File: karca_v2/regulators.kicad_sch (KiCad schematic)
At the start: 27 parts, among them J1 CON_FAN1, J2 Conn_Batt, J3 USB_B_Micro, Q1 AO3401A, SW1 SW_SPST, SW2 SW_SPST, SW3 SW_SPST, U1 TVS1400DRV

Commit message: fixed pmos
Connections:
- net +5V: now also Q1.2 (S); no longer Q1.3 (D)
- net at D4.2 (A), J3.1 (VBUS), TP5.1: now also Q1.3 (D); no longer Q1.2 (S)
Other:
- moved on the sheet: Q1
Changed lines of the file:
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@@
     )
   )
-  (symbol (lib_id "Simulation_SPICE:PMOS") (at 381 157.48 270) (unit 1)
+  (symbol (lib_id "Simulation_SPICE:PMOS") (at 381 157.48 90) (mirror x) (unit 1)
     (in_bom yes) (on_board yes) (dnp no)
     (property "Reference" "Q1" (at 381 163.957 90)
@@
       (effects (font (size 1.27 1.27)))
     )
-    (property "Footprint" "AO3401A:SOT23-3" (at 383.54 162.56 0)
+    (property "Footprint" "AO3401A:SOT23-3" (at 378.46 162.56 0)
       (effects (font (size 1.27 1.27)) hide)
     )
-    (property "Datasheet" "https://ngspice.sourceforge.io/docs/ngspice-manual.pdf" (at 368.3 157.48 0)
+    (property "Datasheet" "https://ngspice.sourceforge.io/docs/ngspice-manual.pdf" (at 393.7 157.48 0)
       (effects (font (size 1.27 1.27)) hide)
     )
-    (property "Sim.Device" "PMOS" (at 363.855 157.48 0)
+    (property "Sim.Device" "PMOS" (at 398.145 157.48 0)
       (effects (font (size 1.27 1.27)) hide)
     )
-    (property "Sim.Type" "VDMOS" (at 361.95 157.48 0)
+    (property "Sim.Type" "VDMOS" (at 400.05 157.48 0)
       (effects (font (size 1.27 1.27)) hide)
     )
-    (property "Sim.Pins" "1=D 2=G 3=S" (at 365.76 157.48 0)
+    (property "Sim.Pins" "1=D 2=G 3=S" (at 396.24 157.48 0)
       (effects (font (size 1.27 1.27)) hide)
     )

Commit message: Passed all DRC, Added safety jumper to isolate regulators from rest of the board
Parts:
- added JP5: Jumper_3_Bridged12, Connector_PinHeader_2.00mm:PinHeader_1x03_P2.00mm_Vertical, symbol Jumper:Jumper_3_Bridged12
- added R121: 250, Resistor_SMD:R_1206_3216Metric, symbol Device:R_US
- J3: footprint USB-B:GCT_USB3090-XX-X_REVE -> USB-B:USB_Micro-B_Molex-105017-0001
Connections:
- net +5V: now also JP5.3 (B); no longer D5.1 (K), Q1.2 (S)
- net GND: now also R121.2
- new net: JP5.2 (C), R121.1
- new net Jumper: D5.1 (K), JP5.1 (A), Q1.2 (S)
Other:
- note added: "Jumper is used to verify the power supply voltage before connecting it to the rest of the circuit"
- moved on the sheet: C1, C2, D1, D2, D3, D4, D5, F1, J1, J2, J3, MD1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

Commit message: cleaned up documentation. Added production files and BOM. Marked Thermocouple components and THT components as DNP (excluded them from BOM too) to match version sent to JLCPCB for fabrication
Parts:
- removed MD1: OKL-T_6-W12N-C, OKL-T6-W12N:MURATA_OKL-T-6-W12N-C_0, symbol OKL-T/6-W12N-C:OKL-T_6-W12N-C
- added MD1: OKL-T_6-W12N-C, OKL-T_6-W12N-C:MURATA_OKL-T-6-W12N-C_0, symbol karca_lib:OKL-T_6-W12N-C
- added R126: 330, Resistor_SMD:R_1206_3216Metric, symbol Device:R_US
- D1, J1, J2, J3, SW1, SW2, SW3: now not fitted; now left out of the parts list
- JP1: renamed from JP5; now not fitted; now left out of the parts list
- R4: value 1.34k -> 1k
- renumbered R121 to R6
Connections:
- net BAT_OUT: now also MD1.4 (VOUT)
- net GND: now also MD1.3 (1_GROUND), MD1.7 (2_GROUND), R126.2; no longer R4.2
- net at C1.1, SW3.2 (B): now also MD1.2 (VIN)
- net at R4.1: now also MD1.6 (TRIM)
- new net: R126.1, R4.2
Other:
- company: (none) -> Rice Eclipse
- title: (none) -> kARCA 2.0 Engine Control System
- moved on the sheet: C1, C2, D2, D3, D4, D5, F1, Q1, R1, R2, R3, R4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

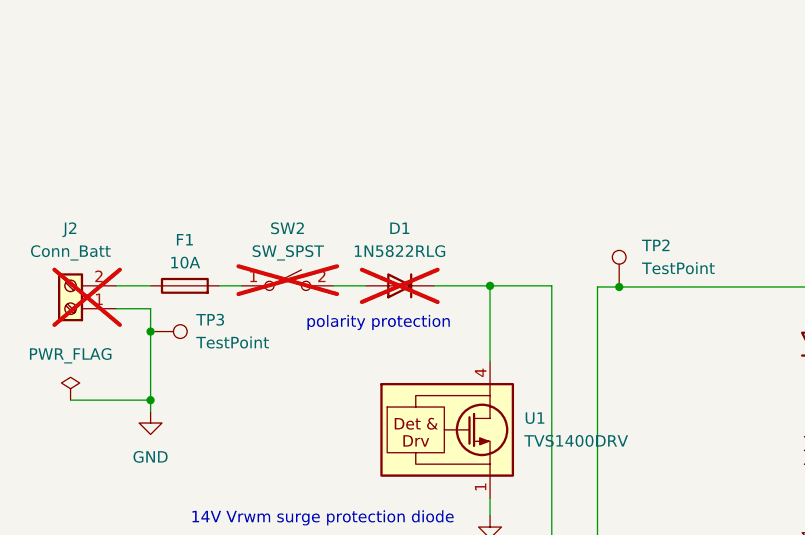
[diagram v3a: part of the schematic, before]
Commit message: updated THT BOM
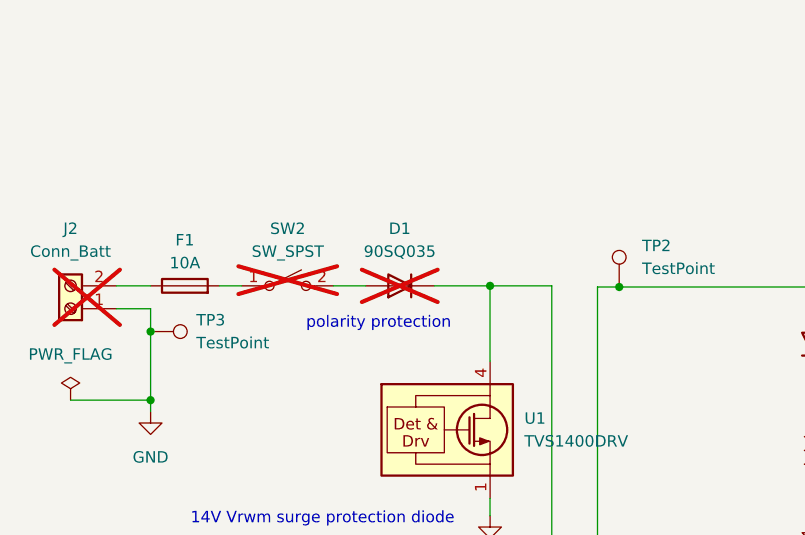
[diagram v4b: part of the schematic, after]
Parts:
- D1: value 1N5822RLG -> 90SQ035
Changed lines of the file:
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@@
       (effects (font (size 1.27 1.27)))
     )
-    (property "Value" "1N5822RLG" (at 58.039 68.199 0)
+    (property "Value" "90SQ035" (at 58.039 68.199 0)
       (effects (font (size 1.27 1.27)))
     )

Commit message: revisions for V2.1
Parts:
- F1: footprint 4628:FUSE_4628 -> custom-footprints:FUSE_4628
- J1, J2: footprint terminal blocks:P-2604-1102 -> custom-footprints:P-2604-1102
- J3: footprint USB-B:USB_Micro-B_Molex-105017-0001 -> custom-footprints:USB_Micro-B_Molex-105017-0001
- JP1: footprint Connector_PinHeader_2.00mm:PinHeader_1x03_P2.00mm_Vertical -> Connector_PinSocket_2.54mm:PinSocket_1x03_P2.54mm_Vertical
- MD1: footprint OKL-T_6-W12N-C:MURATA_OKL-T-6-W12N-C_0 -> custom-footprints:MURATA_OKL-T-6-W12N-C_0
- Q1: footprint AO3401A:SOT23-3 -> custom-footprints:SOT23-3
- SW1, SW2, SW3: footprint 500SSP1S2M2QEA:SW_500SSP1S2M2QEA -> custom-footprints:SW_500SSP1S2M2QEA
